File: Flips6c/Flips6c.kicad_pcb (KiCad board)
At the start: 2 copper layers, 90 x 50 mm, 23 parts, among them CN1 Conn_02x04_Odd_Even, U1 74HCT595, U2 74HCT595, U3 74HCT595

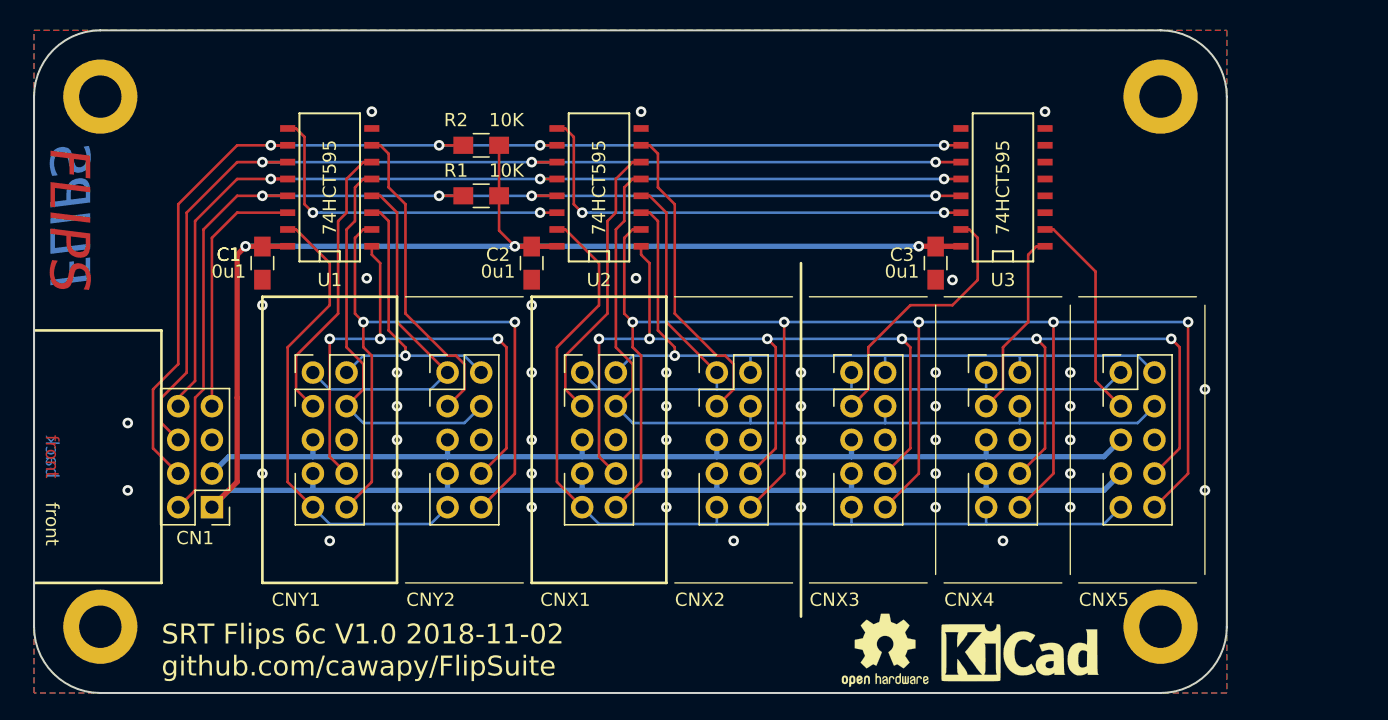
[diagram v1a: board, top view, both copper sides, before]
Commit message: made 12 V net .44 mm, but 5 V net standard 0.2 mm
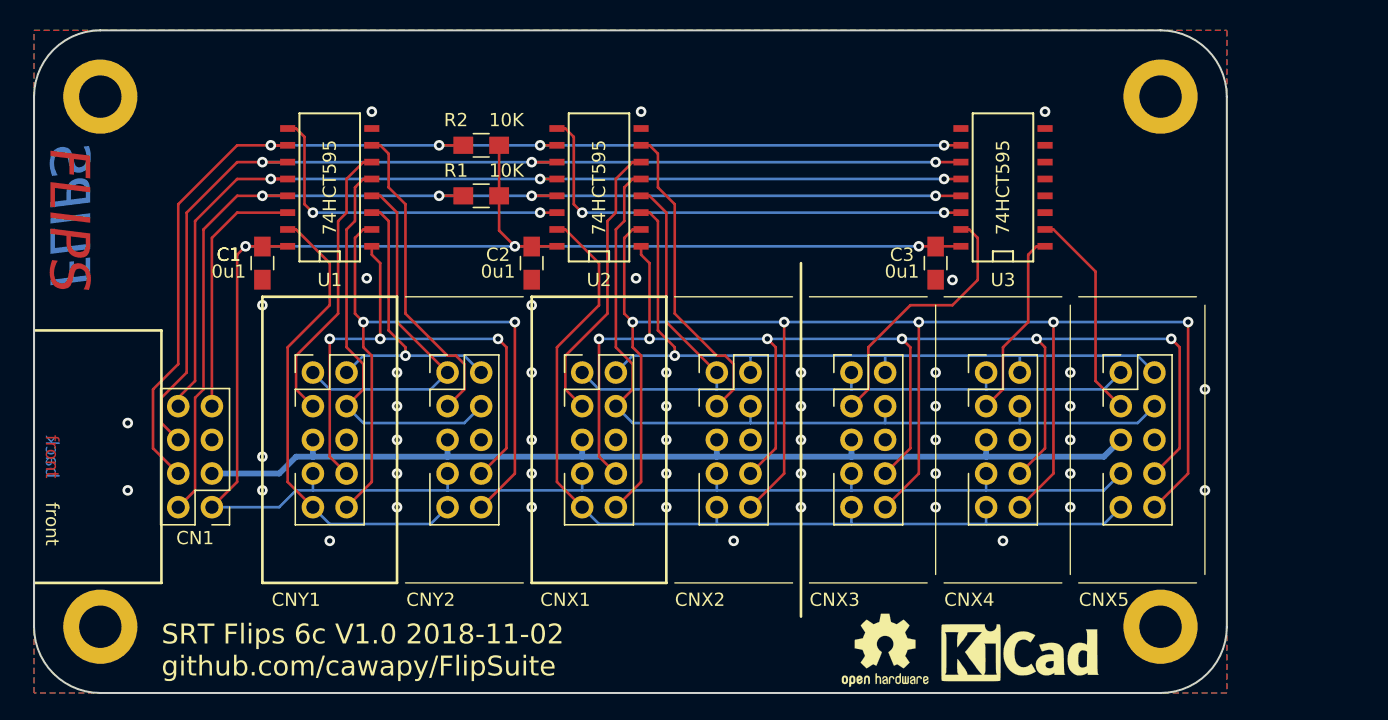
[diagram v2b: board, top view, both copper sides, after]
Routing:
- net GND: vias 45 -> 46
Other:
- net class POW: trace_width 0.4 -> 0.44

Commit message: adding description and pinout
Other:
- board text added: "5V"
- board text added: "CLK"
- board text added: "DIN"
- board text added: "GND"
- board text added: "HV"
- board text added: "LAT"
- board text added: "Serial 2+5 FP2800 Control Port Adaptor"
- board text added: "~OE"
- board text added: "~RST"
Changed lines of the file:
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@@
   (general
     (thickness 1.6)
-    (drawings 53)
+    (drawings 70)
     (tracks 410)
     (zones 0)
@@
   (page A4)
   (layers
-    (0 F.Cu signal)
-    (31 B.Cu signal)
+    (0 F.Cu signal hide)
+    (31 B.Cu signal hide)
     (32 B.Adhes user)
     (33 F.Adhes user)
@@
     (tags "capacitor 0805")
     (attr smd)
-    (fp_text reference C1 (at -0.635 2.54) (layer F.SilkS)
-      (effects (font (size 1 1) (thickness 0.15)))
-    )
-    (fp_text value 0u1 (at 0.635 2.54) (layer F.SilkS)
-      (effects (font (size 1 1) (thickness 0.15)))
-    )
+    (fp_text reference C1 (at -4.826 0.508) (layer F.SilkS)
+      (effects (font (size 1 1) (thickness 0.15)))
+    )
+    (fp_text value 0u1 (at -3.048 0.381) (layer F.SilkS)
+      (effects (font (size 1 1) (thickness 0.15)))
+    )
+    (fp_text user %R (at -4.826 0.508) (layer F.SilkS)
+      (effects (font (size 1 1) (thickness 0.15)))
+    )
+    (fp_line (start -1 0.62) (end -1 -0.62) (layer F.Fab) (width 0.1))
+    (fp_line (start 1 0.62) (end -1 0.62) (layer F.Fab) (width 0.1))
+    (fp_line (start 1 -0.62) (end 1 0.62) (layer F.Fab) (width 0.1))
+    (fp_line (start -1 -0.62) (end 1 -0.62) (layer F.Fab) (width 0.1))
+    (fp_line (start 0.5 -0.85) (end -0.5 -0.85) (layer F.SilkS) (width 0.12))
+    (fp_line (start -0.5 0.85) (end 0.5 0.85) (layer F.SilkS) (width 0.12))
+    (fp_line (start -2.25 -0.88) (end 2.25 -0.88) (layer F.CrtYd) (width 0.05))
+    (fp_line (start -2.25 -0.88) (end -2.25 0.87) (layer F.CrtYd) (width 0.05))
+    (fp_line (start 2.25 0.87) (end 2.25 -0.88) (layer F.CrtYd) (width 0.05))
     (fp_line (start 2.25 0.87) (end -2.25 0.87) (layer F.CrtYd) (width 0.05))
-    (fp_line (start 2.25 0.87) (end 2.25 -0.88) (layer F.CrtYd) (width 0.05))
-    (fp_line (start -2.25 -0.88) (end -2.25 0.87) (layer F.CrtYd) (width 0.05))
-    (fp_line (start -2.25 -0.88) (end 2.25 -0.88) (layer F.CrtYd) (width 0.05))
-    (fp_line (start -0.5 0.85) (end 0.5 0.85) (layer F.SilkS) (width 0.12))
-    (fp_line (start 0.5 -0.85) (end -0.5 -0.85) (layer F.SilkS) (width 0.12))
-    (fp_line (start -1 -0.62) (end 1 -0.62) (layer F.Fab) (width 0.1))
-    (fp_line (start 1 -0.62) (end 1 0.62) (layer F.Fab) (width 0.1))
-    (fp_line (start 1 0.62) (end -1 0.62) (layer F.Fab) (width 0.1))
-    (fp_line (start -1 0.62) (end -1 -0.62) (layer F.Fab) (width 0.1))
-    (fp_text user %R (at -0.635 2.54) (layer F.SilkS)
-      (effects (font (size 1 1) (thickness 0.15)))
-    )
+    (pad 1 smd rect (at -1.25 0 270) (size 1.5 1.25) (layers F.Cu F.Paste F.Mask)
+      (net 1 +5V))
     (pad 2 smd rect (at 1.25 0 270) (size 1.5 1.25) (layers F.Cu F.Paste F.Mask)
       (net 2 GND))
-    (pad 1 smd rect (at -1.25 0 270) (size 1.5 1.25) (layers F.Cu F.Paste F.Mask)
-      (net 1 +5V))
     (model Capacitors_SMD.3dshapes/C_0805.wrl
       (at (xyz 0 0 0))
@@
       (xy 1.530863 2.420002) (xy 1.583231 2.473048) (xy 2.125049 3.022233) (xy 2.12443 2.935152)) (layer B.SilkS) (width 0.01))
   )
+  (gr_line (start 186.563 79.883) (end 184.912 79.883) (layer F.SilkS) (width 0.1))
+  (gr_line (start 186.563 78.867) (end 186.563 79.883) (layer F.SilkS) (width 0.1))
+  (gr_line (start 179.578 72.009) (end 179.578 79.883) (layer F.SilkS) (width 0.1))
+  (gr_line (start 183.388 77.851) (end 186.563 77.851) (layer F.SilkS) (width 0.1))
+  (gr_line (start 183.388 77.851) (end 183.388 79.883) (layer F.SilkS) (width 0.1))
+  (gr_line (start 186.563 72.009) (end 186.563 77.851) (layer F.SilkS) (width 0.1))
+  (gr_line (start 179.578 72.009) (end 186.563 72.009) (layer F.SilkS) (width 0.1))
+  (gr_line (start 183.388 79.883) (end 179.578 79.883) (layer F.SilkS) (width 0.1))
+  (gr_text DIN (at 186.563 73.279) (layer F.SilkS)
+    (effects (font (size 1 1) (thickness 0.15)) (justify right))
+  )
+  (gr_text GND (at 186.563 75.184) (layer F.SilkS)
+    (effects (font (size 1 1) (thickness 0.15)) (justify right))
+  )
+  (gr_text HV (at 186.563 77.089) (layer F.SilkS)
+    (effects (font (size 1 1) (thickness 0.15)) (justify right))
+  )
+  (gr_text 5V (at 186.563 78.994) (layer F.SilkS)
+    (effects (font (size 1 1) (thickness 0.15)) (justify right))
+  )
+  (gr_text CLK (at 179.578 73.279) (layer F.SilkS)
+    (effects (font (size 1 1) (thickness 0.15)) (justify left))
+  )
+  (gr_text ~OE (at 179.578 78.994) (layer F.SilkS)
+    (effects (font (size 1 1) (thickness 0.15)) (justify left))
+  )
+  (gr_text ~RST (at 179.578 77.089) (layer F.SilkS)
+    (effects (font (size 1 1) (thickness 0.15)) (justify left))
+  )
+  (gr_text LAT (at 179.578 75.184) (layer F.SilkS)
+    (effects (font (size 1 1) (thickness 0.15)) (justify left))
+  )
+  (gr_text "Serial\n2+5\nFP2800\nControl Port\nAdaptor" (at 229.87 66.675) (layer F.SilkS)
+    (effects (font (size 1.5 1.5) (thickness 0.3)))
+  )
   (gr_text back (at 173.355 95.25 270) (layer B.SilkS)

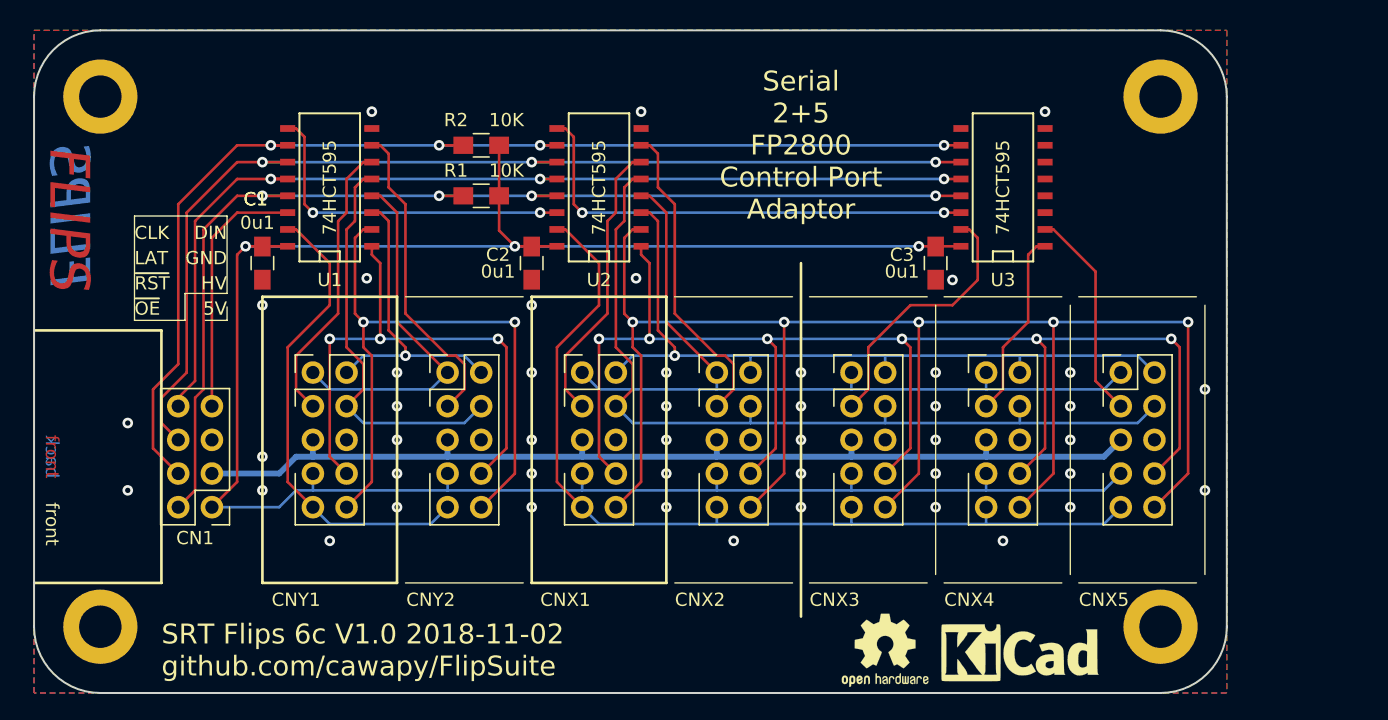
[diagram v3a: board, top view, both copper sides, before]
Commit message: adding 6th UFP2810 port CNX6
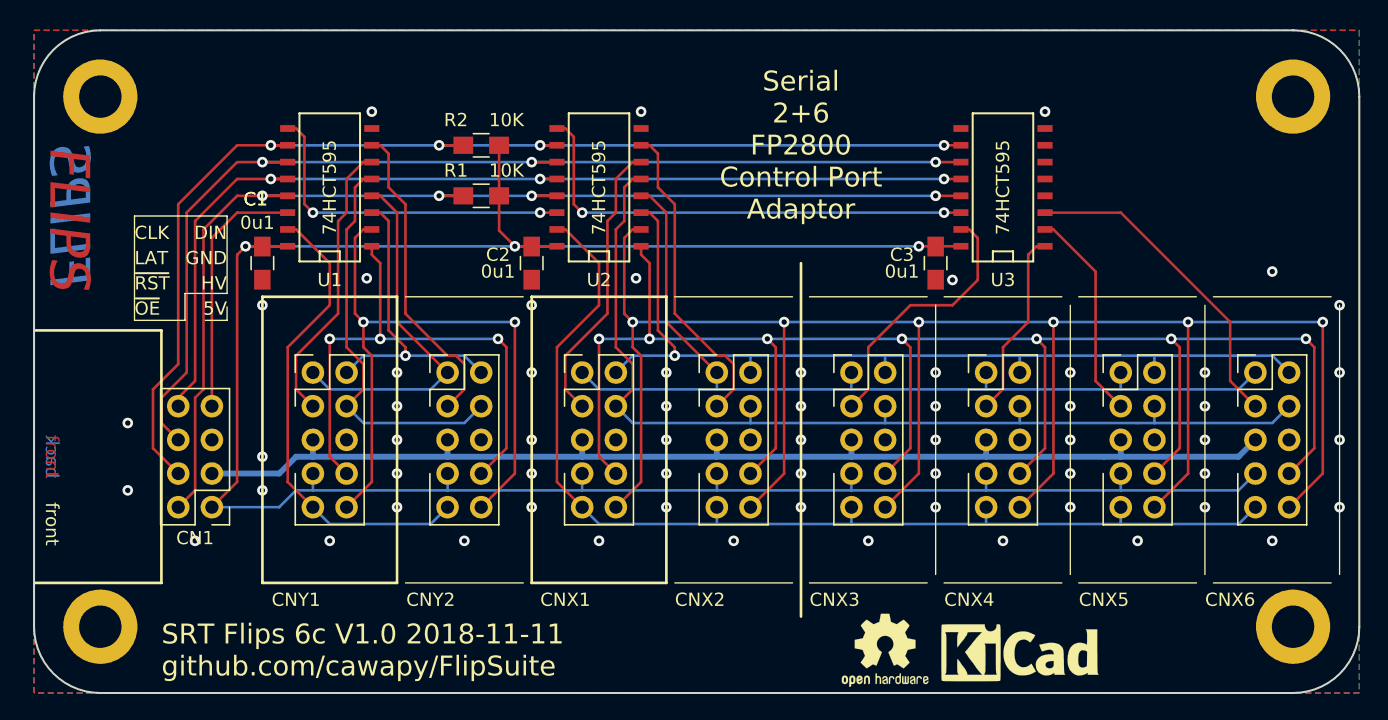
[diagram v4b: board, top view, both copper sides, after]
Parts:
- added CNX6: UFP2810, Own:Pin_Header_Straight_Shrouded_2x05_Pitch2.54mm, F.Cu at (264.2, 83.8)
- moved REF** 10.0 mm to (267.0, 103.0)
- moved REF** 10.0 mm to (267.0, 63.0)
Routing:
- net /XA.2: track 125.2 -> 150.3 mm, vias 5 -> 6
- net /XEN6: track 0.00 -> 24.5 mm
- net /XA.1: track 106.0 -> 127.3 mm, vias 6 -> 7
- net /XB.1: track 61.6 -> 73.0 mm
- net /XA.0: track 70.2 -> 81.7 mm
- net +5V: track 166.5 -> 178.0 mm
- net +12V: track 77.3 -> 88.7 mm
- net /XB.0: track 57.7 -> 69.2 mm
- net /XDAT: track 64.9 -> 76.3 mm
- net GND: vias 46 -> 60
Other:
- board size 90 x 50 mm -> 100 x 50 mm
- board text added: "SRT Flips 6c V1.0 2018-11-11 github.com/cawapy/FlipSuite"
- board text added: "Serial 2+6 FP2800 Control Port Adaptor"
- board text removed: "SRT Flips 6c V1.0 2018-11-02 github.com/cawapy/FlipSuite"
- board text removed: "Serial 2+5 FP2800 Control Port Adaptor"

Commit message: Fixing values to read more friendly, including tech agnostic 74595
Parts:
- C1, C2, C3: value 0u1 -> 0µ1
- R1, R2: value 10K -> 10k
- U1, U2, U3: value 74HCT595 -> 74595
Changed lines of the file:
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@@
       (effects (font (size 1 1) (thickness 0.15)))
     )
-    (fp_text value 0u1 (at -3.048 0.381) (layer F.SilkS)
+    (fp_text value 0µ1 (at -3.048 0.381) (layer F.SilkS)
       (effects (font (size 1 1) (thickness 0.15)))
     )
@@
       (effects (font (size 1 1) (thickness 0.15)))
     )
-    (fp_text value 0u1 (at 0.635 2.54) (layer F.SilkS)
+    (fp_text value 0µ1 (at 0.635 2.54) (layer F.SilkS)
       (effects (font (size 1 1) (thickness 0.15)))
     )
@@
       (effects (font (size 1 1) (thickness 0.15)))
     )
-    (fp_text value 0u1 (at 0.635 2.54) (layer F.SilkS)
+    (fp_text value 0µ1 (at 0.635 2.54) (layer F.SilkS)
       (effects (font (size 1 1) (thickness 0.15)))
     )
@@
       (effects (font (size 1 1) (thickness 0.15)))
     )
-    (fp_text value 10K (at 1.905 -1.905) (layer F.SilkS)
+    (fp_text value 10k (at 1.905 -1.905) (layer F.SilkS)
       (effects (font (size 1 1) (thickness 0.15)))
     )
@@
       (effects (font (size 1 1) (thickness 0.15)))
     )
-    (fp_text value 10K (at 1.905 -1.905) (layer F.SilkS)
+    (fp_text value 10k (at 1.905 -1.905) (layer F.SilkS)
       (effects (font (size 1 1) (thickness 0.15)))
     )
@@
       (effects (font (size 1 1) (thickness 0.15)))
     )
-    (fp_text value 74HCT595 (at 0 0 90) (layer F.SilkS)
+    (fp_text value 74595 (at 6.985 0 180) (layer F.SilkS)
       (effects (font (size 1 1) (thickness 0.15)))
     )
@@
       (effects (font (size 1 1) (thickness 0.15)))
     )
-    (fp_text value 74HCT595 (at 0 0 90) (layer F.SilkS)
+    (fp_text value 74595 (at 6.985 0 180) (layer F.SilkS)
       (effects (font (size 1 1) (thickness 0.15)))
     )
@@
       (effects (font (size 1 1) (thickness 0.15)))
     )
-    (fp_text value 74HCT595 (at 0 0 90) (layer F.SilkS)
-      (effects (font (size 1 1) (thickness 0.15)))
-    )
+    (fp_text value 74595 (at 6.985 0 180) (layer F.SilkS)
+      (effects (font (size 1 1) (thickness 0.15)))
+    )
